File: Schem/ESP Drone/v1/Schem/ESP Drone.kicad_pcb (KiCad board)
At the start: 2 copper layers, 90.1 x 65.1 mm, 81 parts, among them J1 Micro_SD_Card, J2 GEPRC M10 FPV, J3 Conn_01x03_Pin, J4 Conn_01x03_Pin, J5 Conn_01x03_Pin, J6 Conn_01x03_Pin, J7 Conn_Coaxial, U1 ESP32-S2-WROVER, U2 TPS563200, U3 MPU-6050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

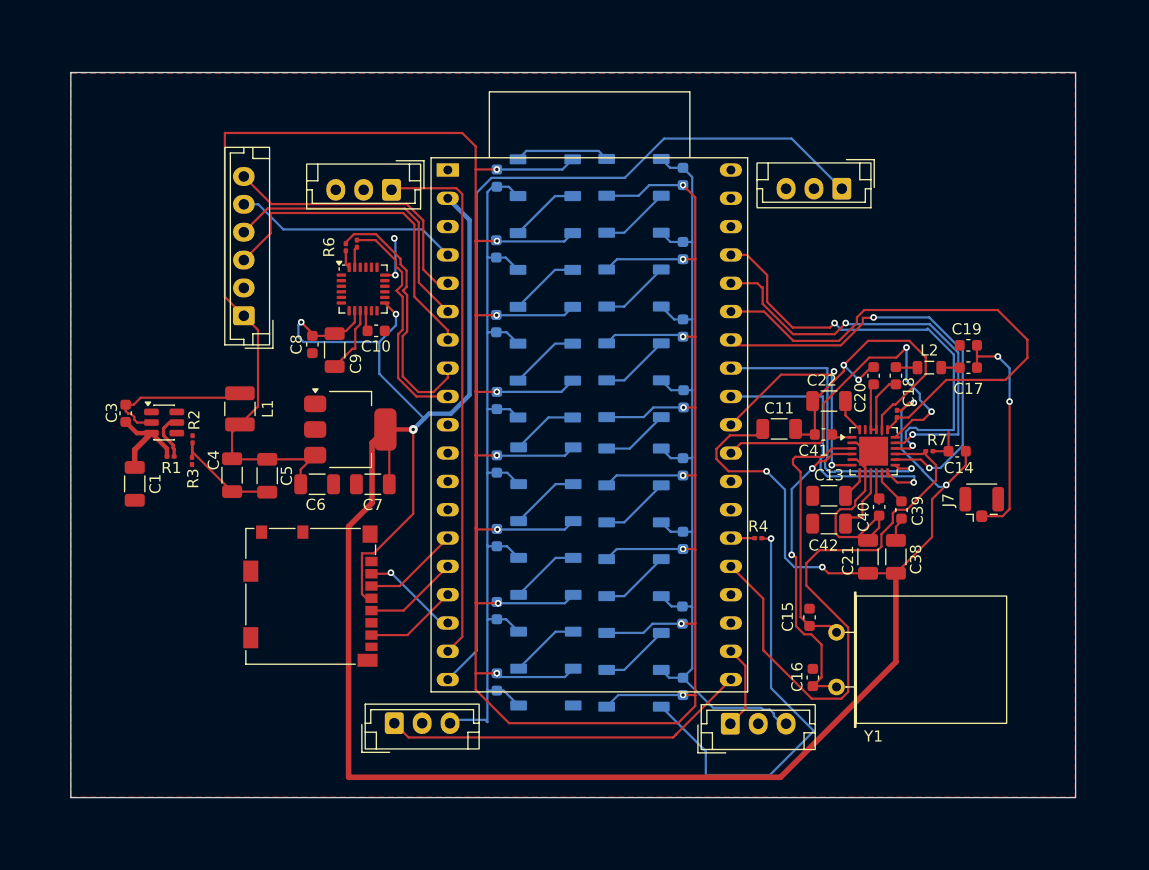
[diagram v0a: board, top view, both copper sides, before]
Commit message: feat: BMP280, LoRa-Protokoll, i18n, Blackbox, Pre-flight Check
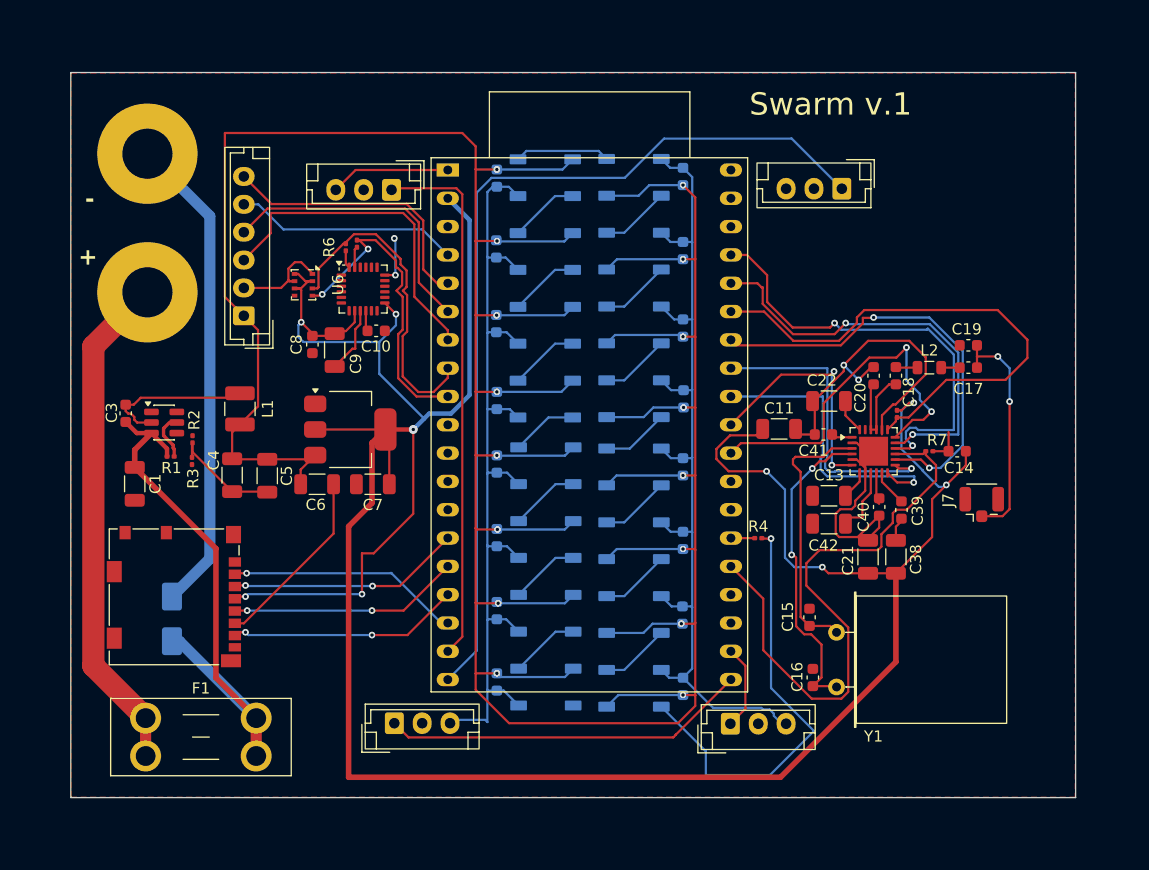
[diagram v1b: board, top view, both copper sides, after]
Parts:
- added D17: SMAJ22A, Diode_SMD:D_SMA, B.Cu at (106.4, 98.7)
- added F1: Fuse, Fuse:Fuseholder_Blade_Mini_Keystone_3568, F.Cu at (104.0, 107.5)
- added J8: Conn_01x01_Pin, Library:high power throu hole, F.Cu at (104.2, 69.3)
- added J9: Conn_01x01_Pin, Library:high power throu hole, F.Cu at (104.2, 56.9)
- added U6: BMP280, Package_LGA:Bosch_LGA-8_2x2.5mm_P0.65mm_ClockwisePinNumbering, F.Cu at (118.2, 68.7)
- moved J1 12.3 mm to (106.6, 96.7)
- moved G*** 2.34 mm to (175.4, 59.5)
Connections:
- net VIN renamed Net-(D17-A1)
- U1 pad 24: Trans RESET -> unconnected-(U1-IO21-Pad24)
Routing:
- net GND: track 234.1 -> 314.2 mm
- net VIN: track 0.00 -> 45.6 mm
- net Net-(D17-A1): track 9.10 -> 49.9 mm
- net + 3.3v: track 228.1 -> 252.3 mm, vias 7 -> 9
- net SD DAT0: track 8.35 -> 20.9 mm, vias 0 -> 2
- net SD CKL: track 8.49 -> 20.9 mm, vias 0 -> 2
- net SD CMD: track 8.63 -> 21.0 mm, vias 0 -> 2
- net SD DAT3/CD: track 8.76 -> 21.1 mm
- net SCL MPU: track 20.9 -> 29.1 mm, vias 0 -> 2
- net SDA MPU: track 23.5 -> 29.1 mm
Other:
- board text added: "+"
- board text added: "-"

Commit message: Exe installer added
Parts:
- added REF**: MountingHole_3.2mm_M3, MountingHole:MountingHole_3.2mm_M3, F.Cu at (97.3, 49.7)
- added REF**: MountingHole_3.2mm_M3, MountingHole:MountingHole_3.2mm_M3, F.Cu at (97.3, 114.7)
- added REF**: MountingHole_3.2mm_M3, MountingHole:MountingHole_3.2mm_M3, F.Cu at (187.4, 114.7)
- added REF**: MountingHole_3.2mm_M3, MountingHole:MountingHole_3.2mm_M3, F.Cu at (187.4, 49.7)
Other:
- board size 90.1 x 65.1 mm -> 99.1 x 74 mm
